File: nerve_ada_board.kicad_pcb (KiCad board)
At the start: 4 copper layers, 120 x 120 mm, 64 parts, among them J10 CAN1, J11 CAN2, J2 TC2050-IDC, J3 2171750001, J5 WS2812B, J6 Camera, J7 PA4-7, J8 PC1-3, J9 PB4-5, SW1 SPST, SW2 SPST, SW3 SPST, U1 LD1117S33TR_SOT223, U2 STM32F446RET, U3 SAM-M10Q, U4 XBP9B-DMWT-002, U8 TXB0104QPWRQ1, U9 TXB0104QPWRQ1, Y1 8M, Y2 32k768

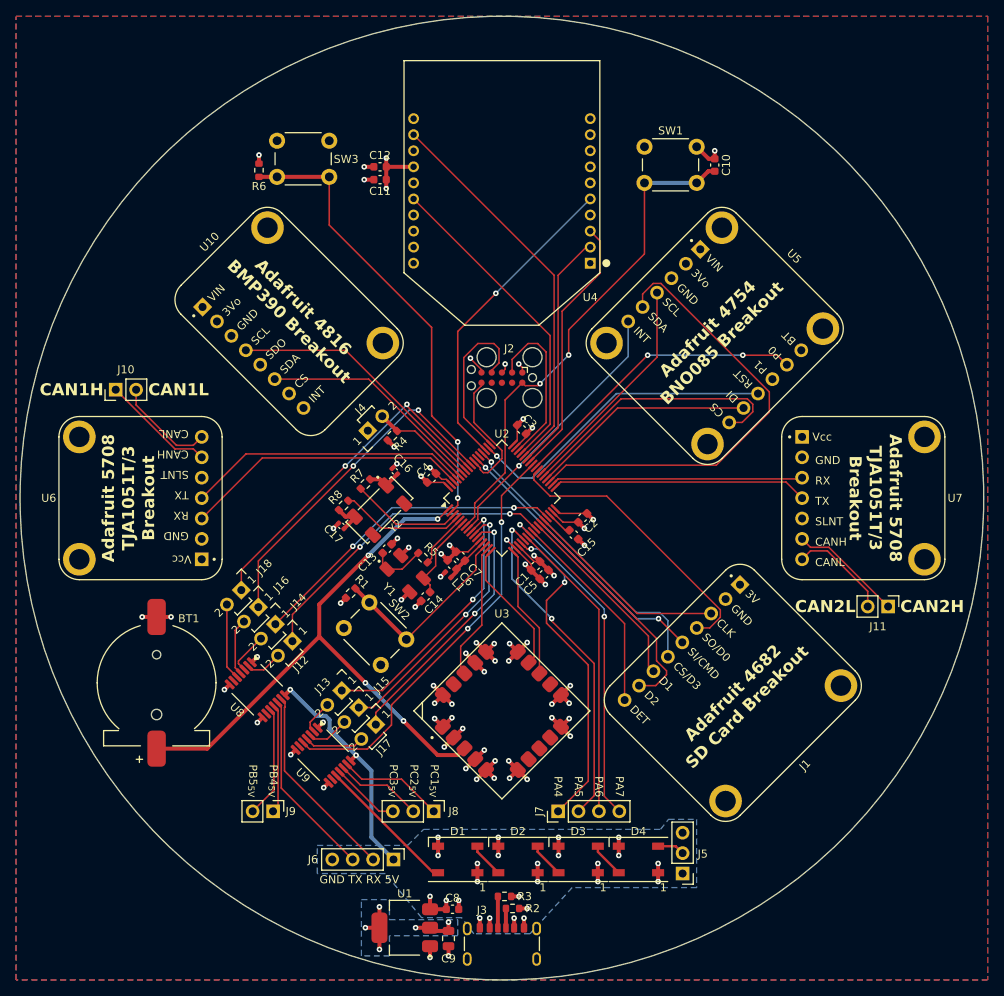
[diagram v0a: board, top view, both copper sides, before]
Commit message: Resolve ERC duplicate labelling warning
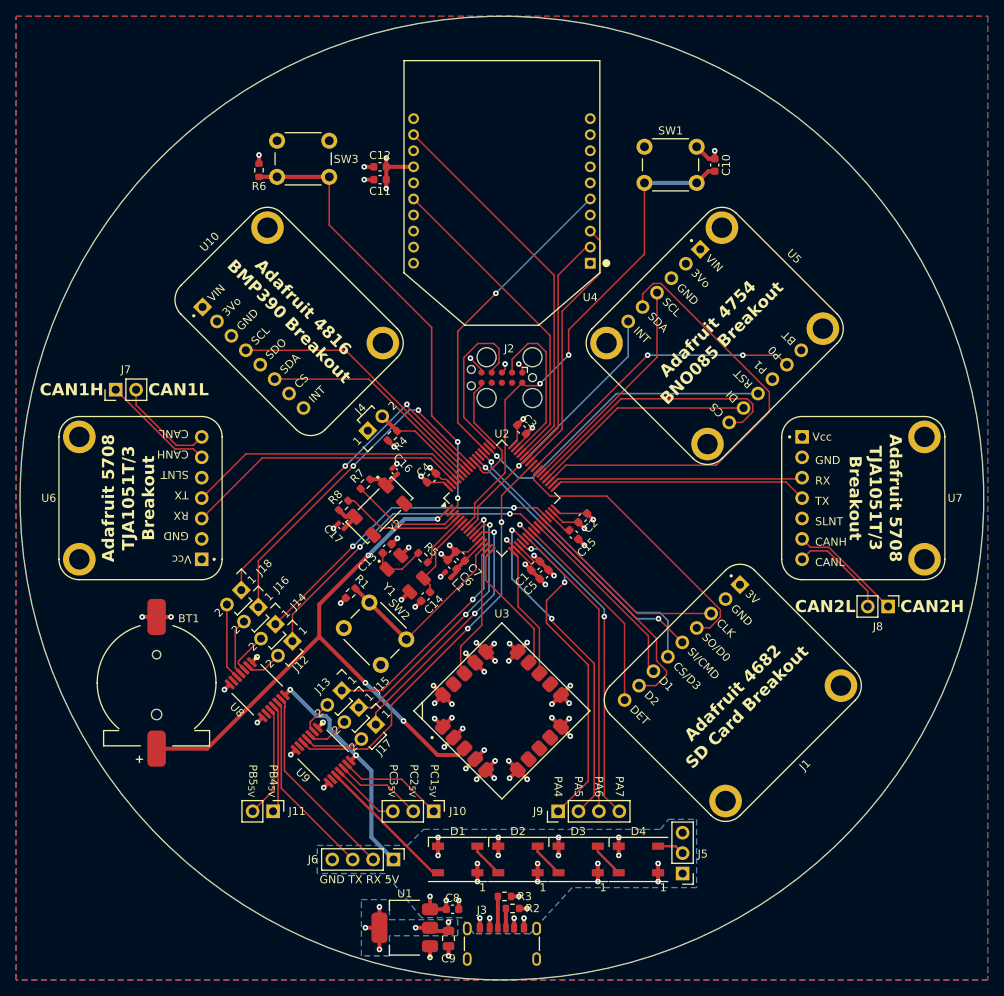
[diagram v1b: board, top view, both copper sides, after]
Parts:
- renumbered J8 to J10, J9 to J11, J10 to J7, J11 to J8, J7 to J9
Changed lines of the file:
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@@
 		(descr "Through hole straight pin header, 1x02, 2.54mm pitch, single row")
 		(tags "Through hole pin header THT 1x02 2.54mm single row")
-		(property "Reference" "J10"
+		(property "Reference" "J7"
 			(at 2.5 1.27 0)
 			(layer "F.SilkS")
@@
 		(fp_arc
 			(start -13.97 -8.89)
-			(mid -12.854074 -11.584074)
+			(mid -12.854073 -11.584073)
 			(end -10.16 -12.7)
 			(stroke
@@
 		(descr "Through hole straight pin header, 1x03, 2.54mm pitch, single row")
 		(tags "Through hole pin header THT 1x03 2.54mm single row")
-		(property "Reference" "J8"
-			(at 0 -2.475 0)
+		(property "Reference" "J10"
+			(at 0 -3 0)
 			(layer "F.SilkS")
 			(effects
@@
 		(descr "Through hole straight pin header, 1x02, 2.54mm pitch, single row")
 		(tags "Through hole pin header THT 1x02 2.54mm single row")
-		(property "Reference" "J9"
-			(at 0 -2.2 0)
+		(property "Reference" "J11"
+			(at 0 -3 0)
 			(layer "F.SilkS")
 			(effects
@@
 		(descr "Through hole straight pin header, 1x02, 2.54mm pitch, single row")
 		(tags "Through hole pin header THT 1x02 2.54mm single row")
-		(property "Reference" "J11"
+		(property "Reference" "J8"
 			(at 2.5 1.27 180)
 			(layer "F.SilkS")
@@
 		(fp_arc
 			(start -13.97 -8.889999)
-			(mid -12.854074 -11.584074)
+			(mid -12.854073 -11.584073)
 			(end -10.159999 -12.7)
 			(stroke
@@
 		(descr "Through hole straight pin header, 1x04, 2.54mm pitch, single row")
 		(tags "Through hole pin header THT 1x04 2.54mm single row")
-		(property "Reference" "J7"
-			(at 0 -2.33 90)
+		(property "Reference" "J9"
+			(at 0 -2.5 0)
 			(layer "F.SilkS")
 			(effects

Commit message: Flight ready alpha and update components
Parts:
- removed the J12 at (121.5, 123.7)
- removed J13, J14, J15, J16, J17, J18: ~, common:harwin_2p_2-54_jumper_closed
- removed the J5 at (171.0, 151.8)
- added J3: 472192001, common:molex_472192001_microsd_hinge, F.Cu at (172.5, 135.5)
- added J6: WS2812B, Connector_PinHeader_2.54mm:PinHeader_1x02_P2.54mm_Vertical, F.Cu at (105.8, 121.8)
- added R1: 47k, Resistor_SMD:R_0603_1608Metric, F.Cu at (162.8, 133.0)
- added R2: 47k, Resistor_SMD:R_0603_1608Metric, F.Cu at (162.8, 134.8)
- added R3: 47k, Resistor_SMD:R_0603_1608Metric, F.Cu at (162.8, 136.5)
- added R4: 47k, Resistor_SMD:R_0603_1608Metric, F.Cu at (162.8, 138.2)
- added R5: 47k, Resistor_SMD:R_0603_1608Metric, F.Cu at (162.8, 140.0)
- added R6: 10k, Resistor_SMD:R_0603_1608Metric, F.Cu at (186.1, 131.6)
- J1: footprint adafruit:adafruit_4682_sdio_card -> common:harwin_2p_2-54_jumper_open
- moved R7 62.8 mm to (190.3, 100.5), turned to 180 degrees
- moved SW2 60.8 mm to (189.5, 98.2), turned to 90 degrees
- moved D4 59.0 mm to (110.6, 128.3), turned to -45 degrees
- moved D3 45.2 mm to (115.9, 133.6), turned to -45 degrees
- moved SW3 41.6 mm to (103.0, 98.2), turned to 90 degrees
- moved R12 38.1 mm to (106.7, 100.5), turned to 0 degrees
- moved C10 34.1 mm to (159.2, 93.8), turned to 0 degrees
- moved J11 33.0 mm to (152.5, 138.5), turned to 180 degrees
- moved D2 31.4 mm to (121.2, 138.9), turned to -45 degrees
- moved U9 30.5 mm to (146.8, 139.0), turned to -90 degrees
- moved SW1 28.5 mm to (154.0, 87.0)
- moved C12 23.9 mm to (137.4, 87.3), turned to 0 degrees
- moved J9 23.1 mm to (159.2, 121.2), turned to 0 degrees
- moved BT1 22.6 mm to (128.1, 128.6), turned to 97.5 degrees
- moved C11 20.7 mm to (137.4, 85.7), turned to 0 degrees
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- renumbered J6 to J12, J3 to J4, J4 to J5, R4 to R10, R5 to R11, R6 to R12, R7 to R13, R8 to R14, R1 to R7, R2 to R8, R3 to R9, U9 to U10, U10 to U3, U3 to U4, U4 to U5, U5 to U6, U6 to U7, U7 to U8, U8 to U9
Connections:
- J1 pad 2: GND -> /SDIO_DET
- U10 pad 2: Net-(U9-A1) -> /PC1
- U10 pad 3: Net-(U9-A2) -> /PC2
- U10 pad 4: Net-(U9-A3) -> /PC3
- U9 pad 2: Net-(U8-A1) -> /USART3_RX
- U9 pad 3: Net-(U8-A2) -> /USART3_TX
- U9 pad 4: Net-(U8-A3) -> /PB4
- U9 pad 5: Net-(U8-A4) -> /PB5
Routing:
- net +3.3VBATT: track 75.6 -> 14.0 mm, vias 4 -> 7
- net /SPI2_MISO: track 57.0 -> 15.2 mm
- net Net-(U2-PA0): track 24.7 -> 57.4 mm, vias 0 -> 2
- net /SDIO_CMD: track 35.1 -> 63.1 mm
- net /SDIO_D3: track 36.9 -> 64.7 mm, vias 1 -> 2
- net /NRST: track 63.0 -> 36.4 mm, vias 2 -> 1
- net /SDIO_D2: track 29.3 -> 54.7 mm, vias 0 -> 2
- net /PA5: track 42.1 -> 18.0 mm, vias 2 -> 0
- net /PA4: track 41.1 -> 17.4 mm
- net /GPIO_RADIO_RST: track 39.6 -> 20.6 mm, vias 1 -> 0
- net /PA7: track 42.6 -> 24.2 mm, vias 2 -> 0
- net /CAN2-: track 12.6 -> 30.9 mm
- net /SDIO_DET: track 25.7 -> 43.4 mm, vias 0 -> 2
- net /SDIO_D0: track 35.8 -> 53.5 mm, vias 0 -> 2
- net /PA6: track 37.8 -> 21.1 mm
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- added copper zone on B.Cu, net +3.3VBATT
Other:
- board size 120 x 120 mm -> 100 x 100 mm
- board text added: "5V RX TX GND"
- board text added: "CAN1"
- board text added: "CAN2"
- board text added: "GND RGB"
- board text added: "H"
- board text added: "L"
- board text removed: "CAN1H"
- board text removed: "CAN1L"
- board text removed: "CAN2H"
- board text removed: "CAN2L"
- board text removed: "GND TX RX 5V"

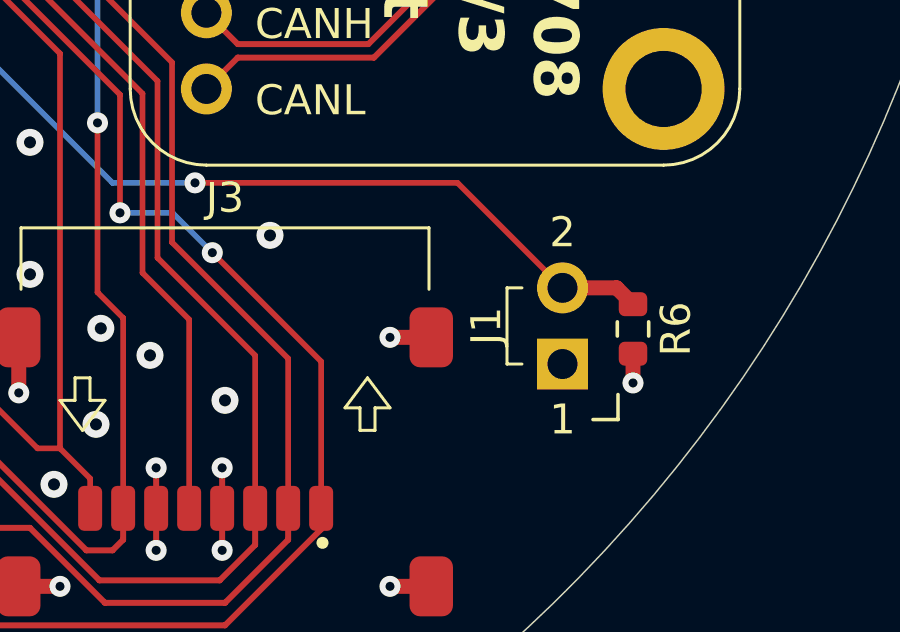
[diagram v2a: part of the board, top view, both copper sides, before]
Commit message: Fix SDIO card detect for active low
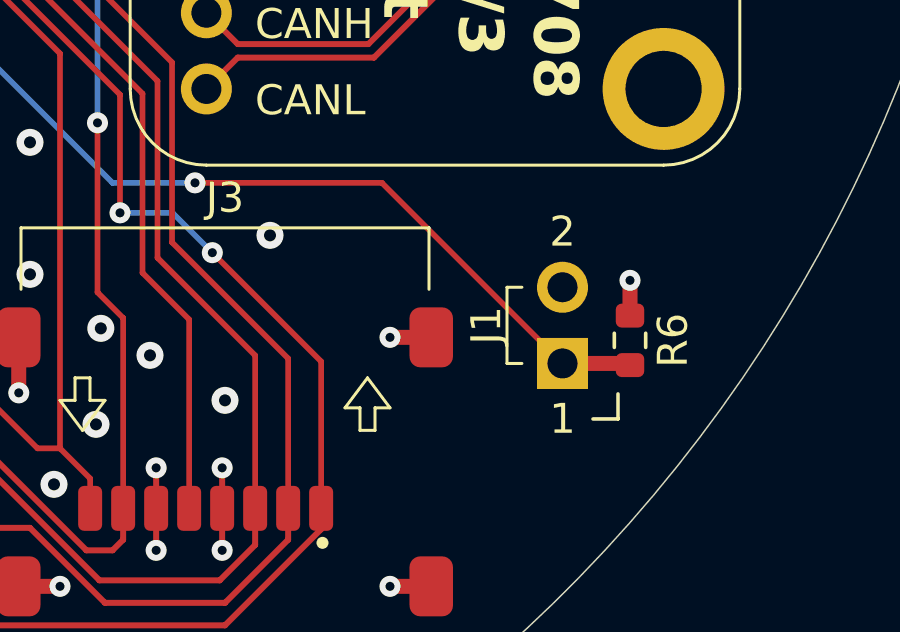
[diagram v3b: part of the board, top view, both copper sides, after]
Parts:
- moved R6 0.39 mm to (186.0, 132.0)
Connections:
- J1 pad 1: +3V3 -> /SDIO_DET
- J1 pad 2: /SDIO_DET -> GND
- R6 pad 1: /SDIO_DET -> +3V3
- R6 pad 2: GND -> /SDIO_DET
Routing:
- net +3V3: track 65.5 -> 66.6 mm, vias 33 -> 34
- net GND: track 115.8 -> 114.9 mm, vias 229 -> 228
- net /SDIO_DET: track 43.4 -> 44.1 mm

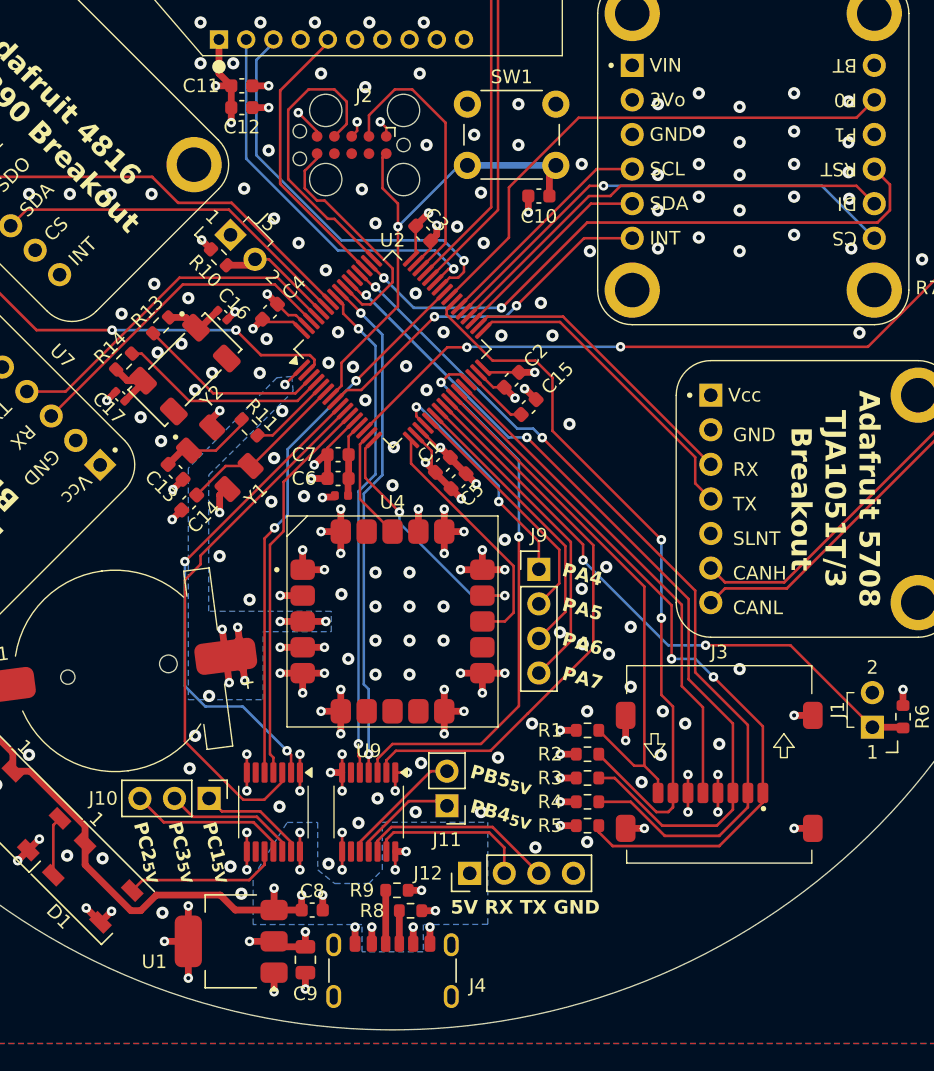
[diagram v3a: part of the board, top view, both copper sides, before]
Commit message: Swap to LD39150DT33-R regulator
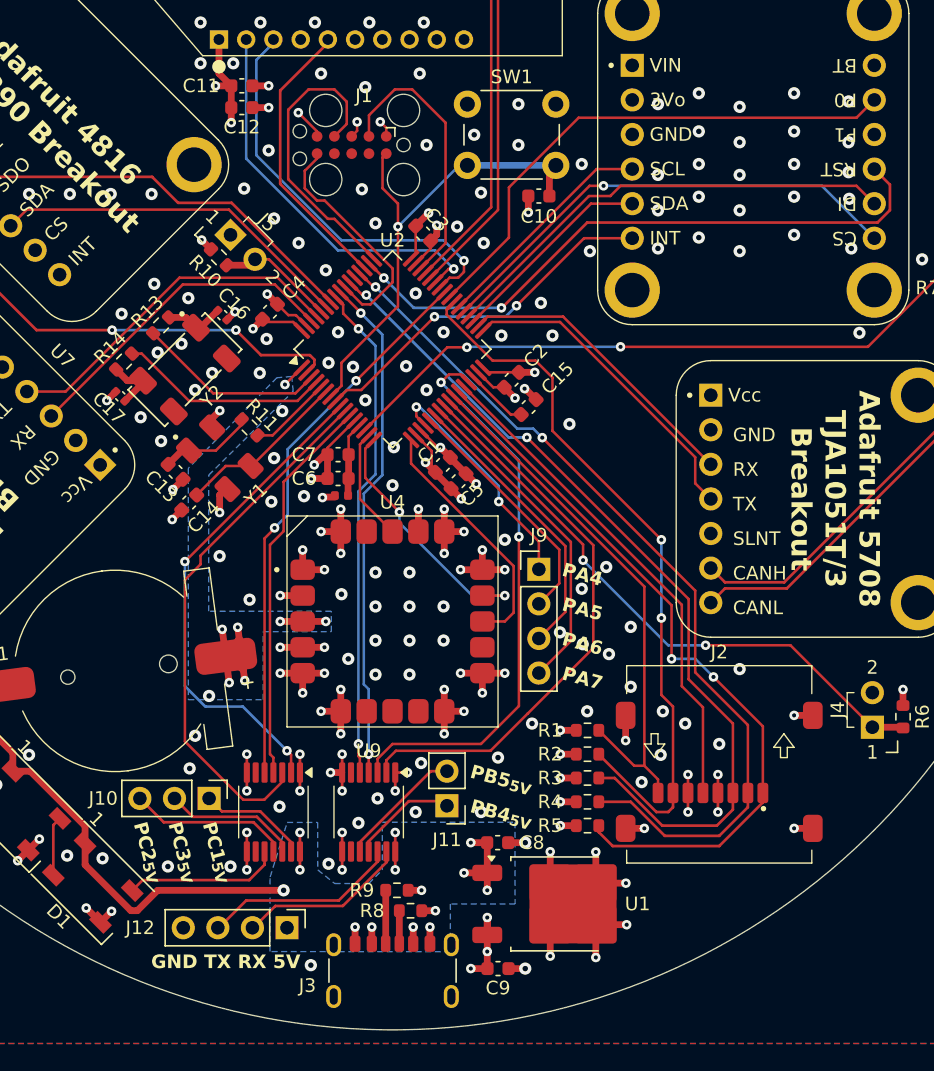
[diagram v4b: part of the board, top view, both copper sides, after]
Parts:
- C8: value 100n -> 1u
- C9: value 10u -> 2u2; footprint Capacitor_SMD:C_0805_2012Metric -> Capacitor_SMD:C_0603_1608Metric
- U1: value LD1117S33TR_SOT223 -> ld39150dt33-r; footprint Package_TO_SOT_SMD:SOT-223-3_TabPin2 -> common:to-252-2_dpak-2-leg
- moved U1 24.0 mm to (160.5, 145.8), turned to 0 degrees
- moved C8 14.5 mm to (156.2, 141.2)
- moved C9 14.2 mm to (156.2, 150.5), turned to 0 degrees
- moved J12 14.0 mm to (140.8, 147.5), turned to -90 degrees
- renumbered J2 to J1, J3 to J2, J4 to J3, J1 to J4
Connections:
- U1 pad 1: GND -> +5V
- U1 pad 2: +3V3 -> GND
- U1 pad 3: +5V -> +3V3
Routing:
- net GND: track 114.9 -> 127.4 mm, vias 228 -> 231
- net +3V3: track 66.6 -> 60.5 mm, vias 34 -> 32
- net +5V: track 55.2 -> 57.3 mm, vias 8 -> 10
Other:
- board text added: "GND TX RX 5V"
- board text removed: "5V RX TX GND"

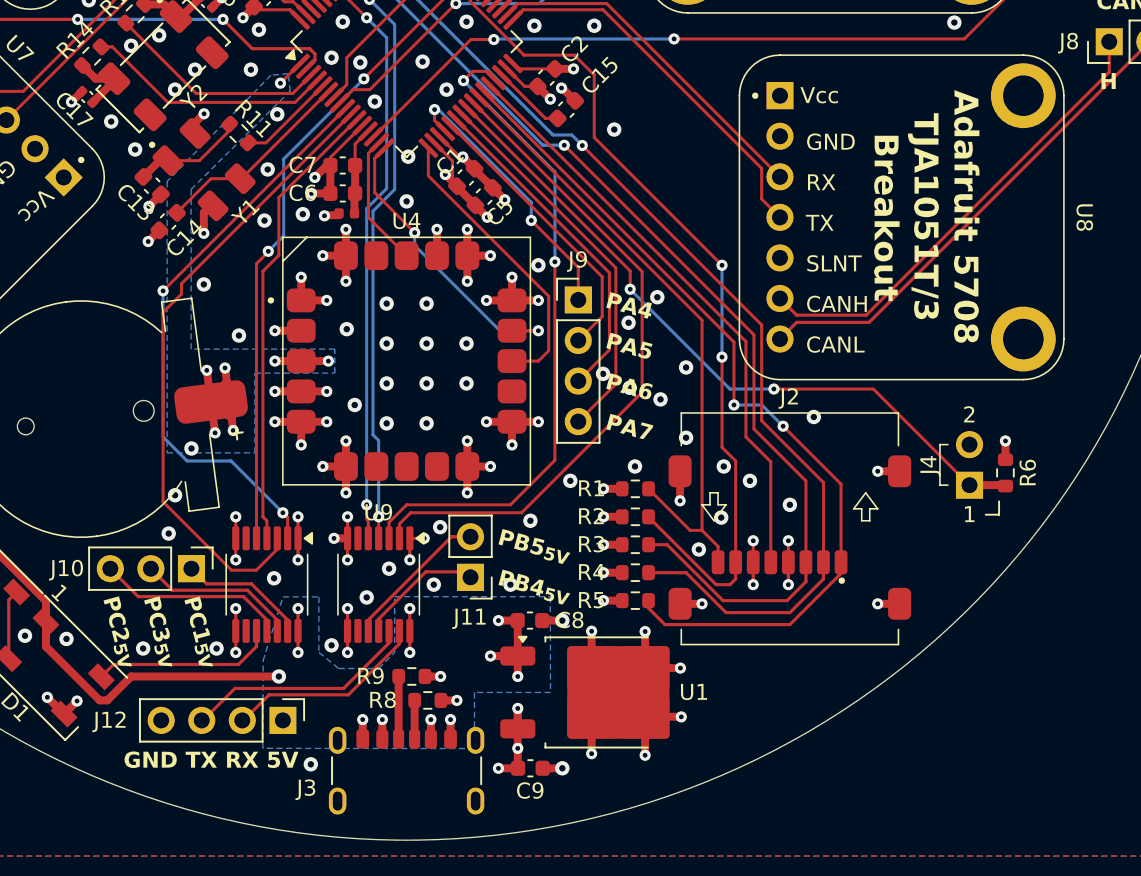
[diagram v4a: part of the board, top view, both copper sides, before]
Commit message: Clean up layout around SDIO
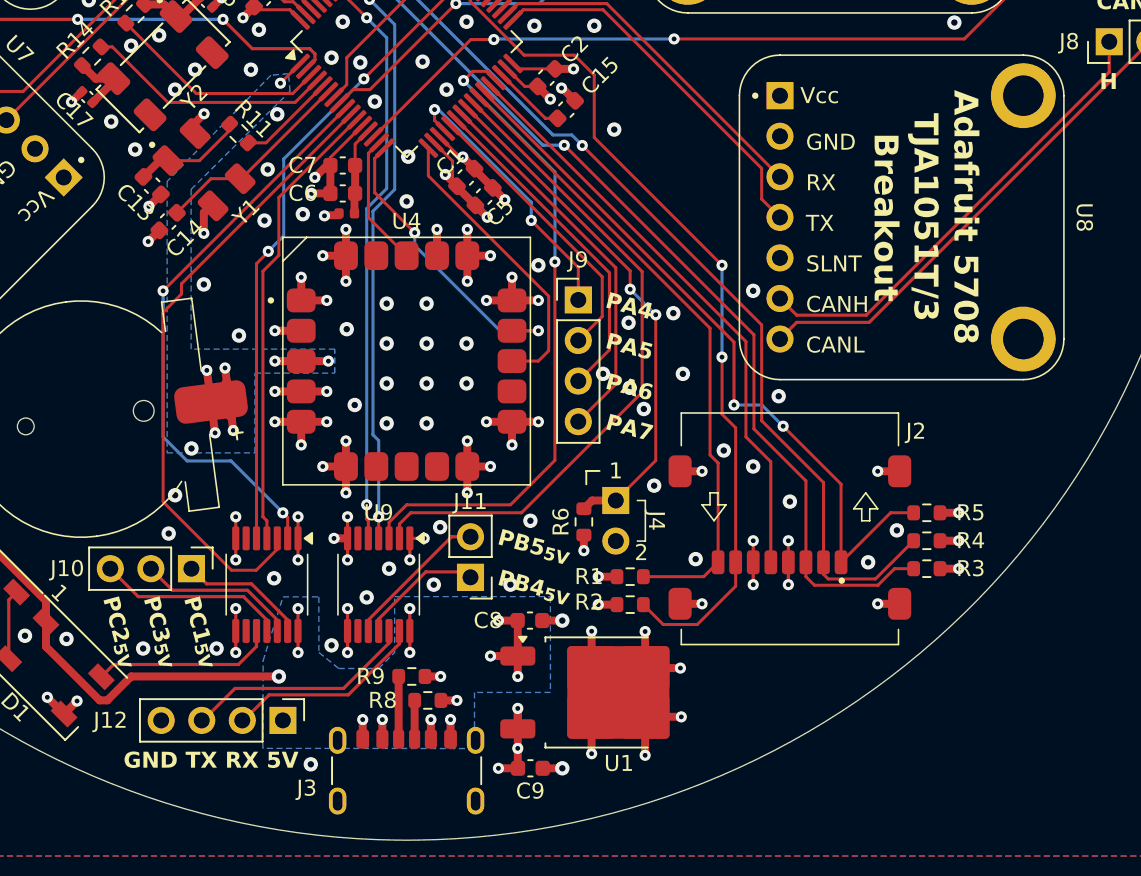
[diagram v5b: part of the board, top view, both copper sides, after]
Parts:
- moved R6 26.6 mm to (159.6, 135.1), turned to 90 degrees
- moved J4 22.4 mm to (161.6, 135.0), turned to -90 degrees
- moved R5 19.1 mm to (181.1, 134.5), turned to 180 degrees
- moved R4 18.4 mm to (181.1, 136.2), turned to 180 degrees
- moved R3 18.3 mm to (181.1, 138.0), turned to 180 degrees
- moved R1 5.51 mm to (162.5, 138.5)
- moved R2 5.51 mm to (162.5, 140.2)
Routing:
- net /SDIO_DET: track 44.1 -> 32.7 mm
- net /SDIO_D2: track 54.7 -> 45.6 mm
- net /SDIO_D3: track 64.7 -> 58.3 mm
- net /SDIO_CMD: track 63.1 -> 58.4 mm
- net /SDIO_D0: track 53.5 -> 54.2 mm
- net /SDIO_D1: track 40.1 -> 40.8 mm
